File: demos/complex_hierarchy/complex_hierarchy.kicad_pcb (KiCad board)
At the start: 2 copper layers, 72 parts, among them P1 CONN_2, P2 CONN_2, P3 CONN_2, P4 CONN_2, P5 CONN_2, P6 CONN_2, Q1 MPAS92, Q2 MPAS42, Q3 MPAS92, Q4 MPAS42, Q5 MPAS92, Q6 MPAS42, Q7 MPAS92, Q8 MPAS42, U1 ICL7660, U2 78L05, U3 LM358N, U4 LM358N

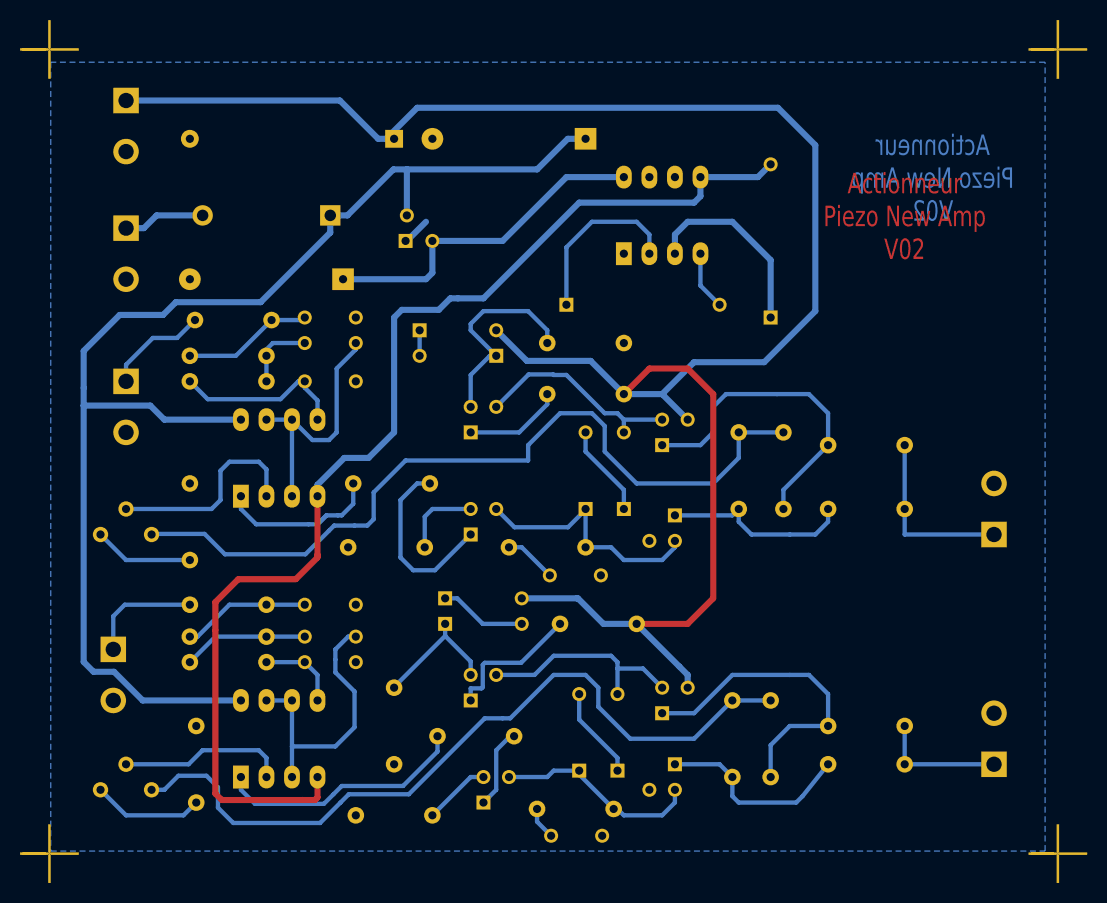
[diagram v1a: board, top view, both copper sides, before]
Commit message: Update demo files. A minor code cleaning.
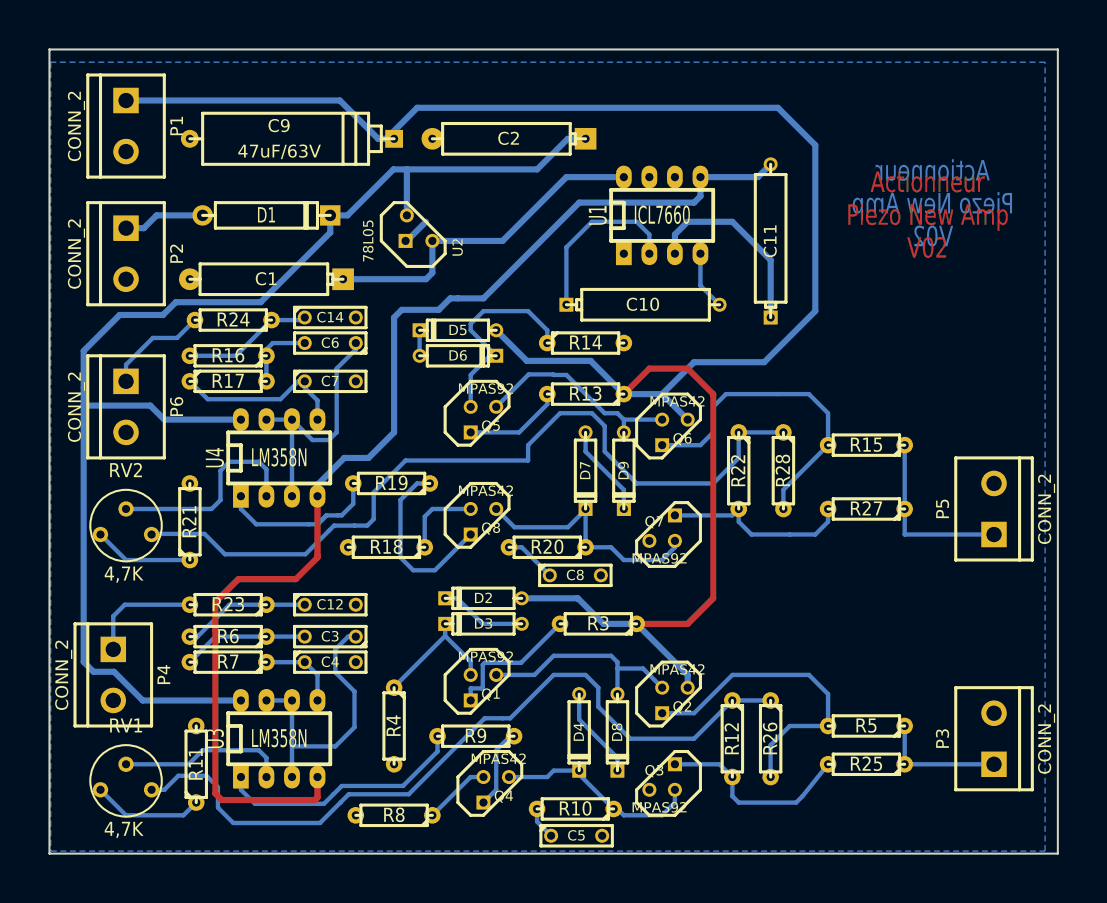
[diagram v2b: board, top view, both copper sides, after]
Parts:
- removed MIRE (x4): *, MIRE
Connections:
- net /ampli_h1 renamed /ampli_ht_vertical/Vpil_0_3,3V
- net /ampli_h2 renamed /ampli_ht_horizontal/Vpil_0_3,3V
- net /ampli_h3 renamed /ampli_ht_vertical/PIEZO_OUT
- net /ampli_h4 renamed /ampli_ht_vertical/PIEZO_IN
- net /ampli_h5 renamed /ampli_ht_horizontal/PIEZO_OUT
- net /ampli_h6 renamed /ampli_ht_horizontal/PIEZO_IN
- net /ampli_h7 renamed /ampli_ht_vertical/S_OUT+
- net /ampli_h8 renamed /ampli_ht_horizontal/S_OUT+
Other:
- board outline added: 100.3 x 80 mm

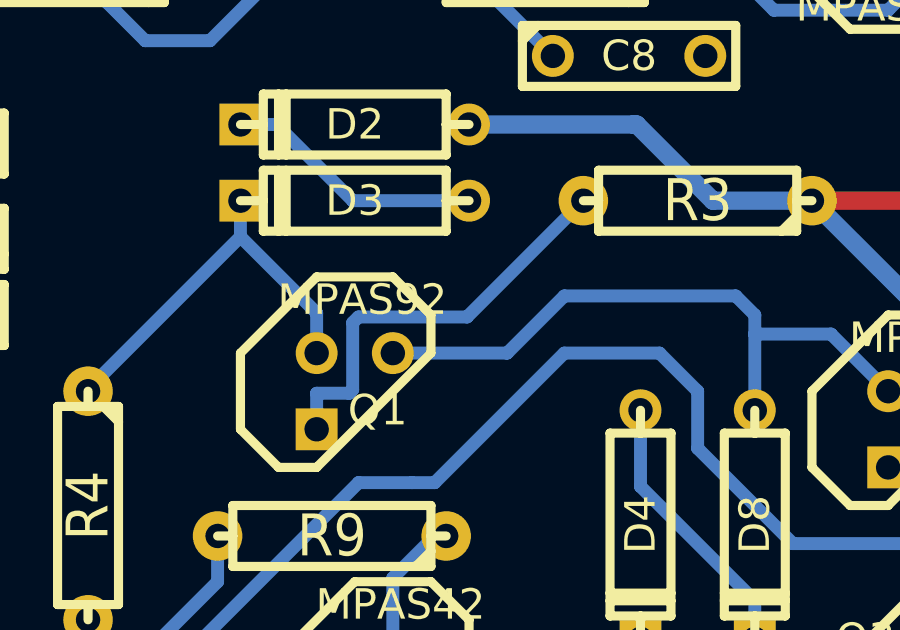
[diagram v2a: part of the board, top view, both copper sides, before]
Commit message: add patch from Cirilo Bernardo, and minor fixes.
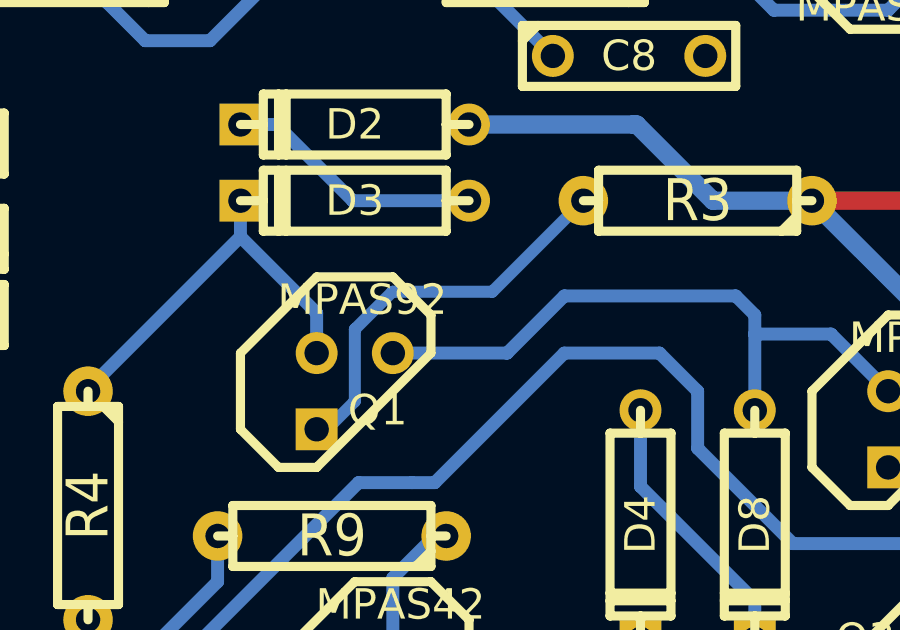
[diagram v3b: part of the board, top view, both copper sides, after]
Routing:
- net Net-(Q1-PadE): track 14.1 -> 13.5 mm
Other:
- net class Default: clearance 0.2794 -> 0.3; trace_width 0.4318 -> 0.4
- net class power: clearance 0.381 -> 0.3; trace_width 0.6096 -> 0.6
- rule trace_clearance: 0.2794 -> 0.3
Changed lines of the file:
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@@
-(kicad_pcb (version 3) (host pcbnew "(2014-01-08 BZR 4616)-product")
+(kicad_pcb (version 3) (host pcbnew "(2014-01-22 BZR 4630)-product")
   (general
     (links 112)
     (no_connects 0)
-    (area 88.163399 51.714399 188.696601 131.927601)
+    (area 84.538458 51.714399 192.321543 131.927601)
     (thickness 1.6002)
     (drawings 6)
-    (tracks 361)
+    (tracks 360)
     (zones 0)
     (modules 68)
@@
   )
   (setup
-    (last_trace_width 0.4318)
-    (trace_clearance 0.2794)
+    (last_trace_width 0.4)
+    (trace_clearance 0.3)
     (zone_clearance 0.508)
     (zone_45_only no)
     (trace_min 0.2032)
-    (segment_width 0.381)
-    (edge_width 0.2032)
+    (segment_width 0.3)
+    (edge_width 0.1)
     (via_size 1.651)
     (via_drill 0.635)
@@
     (uvia_min_size 0.508)
     (uvia_min_drill 0.2032)
-    (pcb_text_width 0.3048)
-    (pcb_text_size 1.524 2.032)
-    (mod_edge_width 0.381)
-    (mod_text_size 1.524 1.524)
-    (mod_text_width 0.3048)
+    (pcb_text_width 0.3)
+    (pcb_text_size 2 2)
+    (mod_edge_width 0.2)
+    (mod_text_size 1 1)
+    (mod_text_width 0.2)
     (pad_size 2.286 2.286)
     (pad_drill 0.8128)
@@
   (net 50 VCC)
   (net_class Default "Ceci est la Netclass par défaut"
-    (clearance 0.2794)
-    (trace_width 0.4318)
+    (clearance 0.3)
+    (trace_width 0.4)
     (via_dia 1.651)
     (via_drill 0.635)
@@
   )
   (net_class power ""
-    (clearance 0.381)
-    (trace_width 0.6096)
+    (clearance 0.3)
+    (trace_width 0.6)
     (via_dia 1.651)
     (via_drill 0.635)
@@
   (segment (start 145.415 89.916) (end 145.415 88.646) (width 0.4318) (layer Cuivre) (net 33) (status 800))
   (segment (start 145.415 88.646) (end 149.225 88.646) (width 0.4318) (layer Cuivre) (net 33) (status 400))
-  (segment (start 135.18896 112.84204) (end 139.065 108.966) (width 0.4318) (layer Cuivre) (net 34) (status 400))
-  (segment (start 131.56692 112.84204) (end 135.18896 112.84204) (width 0.4318) (layer Cuivre) (net 34))
-  (segment (start 131.37642 115.26266) (end 131.37642 113.03254) (width 0.4318) (layer Cuivre) (net 34))
-  (segment (start 130.175 116.586) (end 130.175 115.38458) (width 0.4318) (layer Cuivre) (net 34) (status 800))
-  (segment (start 131.2545 115.38458) (end 131.37642 115.26266) (width 0.4318) (layer Cuivre) (net 34))
-  (segment (start 131.37642 113.03254) (end 131.56692 112.84204) (width 0.4318) (layer Cuivre) (net 34))
-  (segment (start 130.175 115.38458) (end 131.2545 115.38458) (width 0.4318) (layer Cuivre) (net 34))
+  (segment (start 130.175 116.586) (end 130.514 116.586) (width 0.4) (layer Cuivre) (net 34))
+  (segment (start 136.031 112) (end 139.065 108.966) (width 0.4) (layer Cuivre) (net 34))
+  (segment (start 132.7 112) (end 136.031 112) (width 0.4) (layer Cuivre) (net 34))
+  (segment (start 131.44787 113.25213) (end 132.7 112) (width 0.4) (layer Cuivre) (net 34))
+  (segment (start 131.44787 115.65213) (end 131.44787 113.25213) (width 0.4) (layer Cuivre) (net 34))
+  (segment (start 130.514 116.586) (end 131.44787 115.65213) (width 0.4) (layer Cuivre) (net 34))
   (segment (start 160.02 124.206) (end 160.02 121.031) (width 0.4318) (layer Cuivre) (net 35) (status 800))
   (segment (start 161.925 119.126) (end 165.735 119.126) (width 0.4318) (layer Cuivre) (net 35) (status 400))

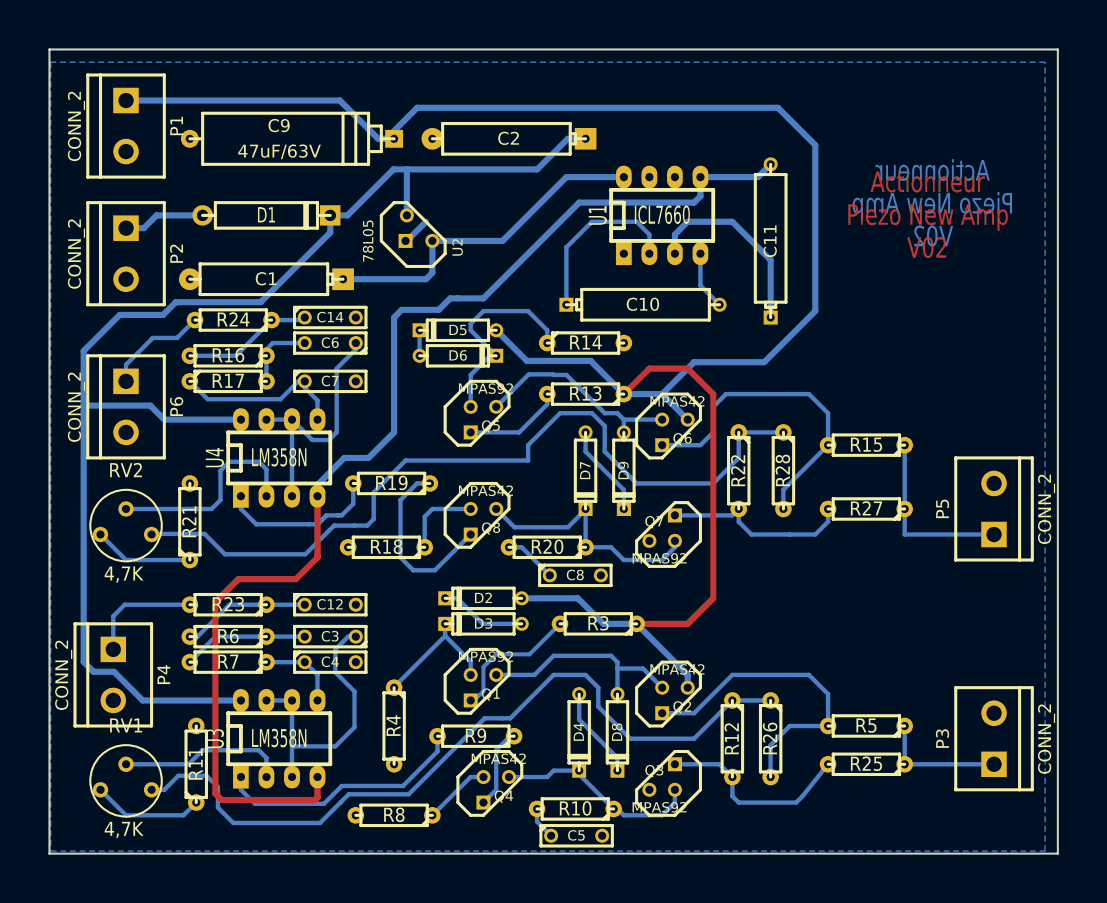
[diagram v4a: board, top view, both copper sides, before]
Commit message: Eeschema: BOM dialog: fix some minor issues when displaying messages. Cvpcb: fix Bug #1470201 (select next/previous unlinked comp and clear links not working well) demo/complex_hierarchy: use our new schematic symbols.
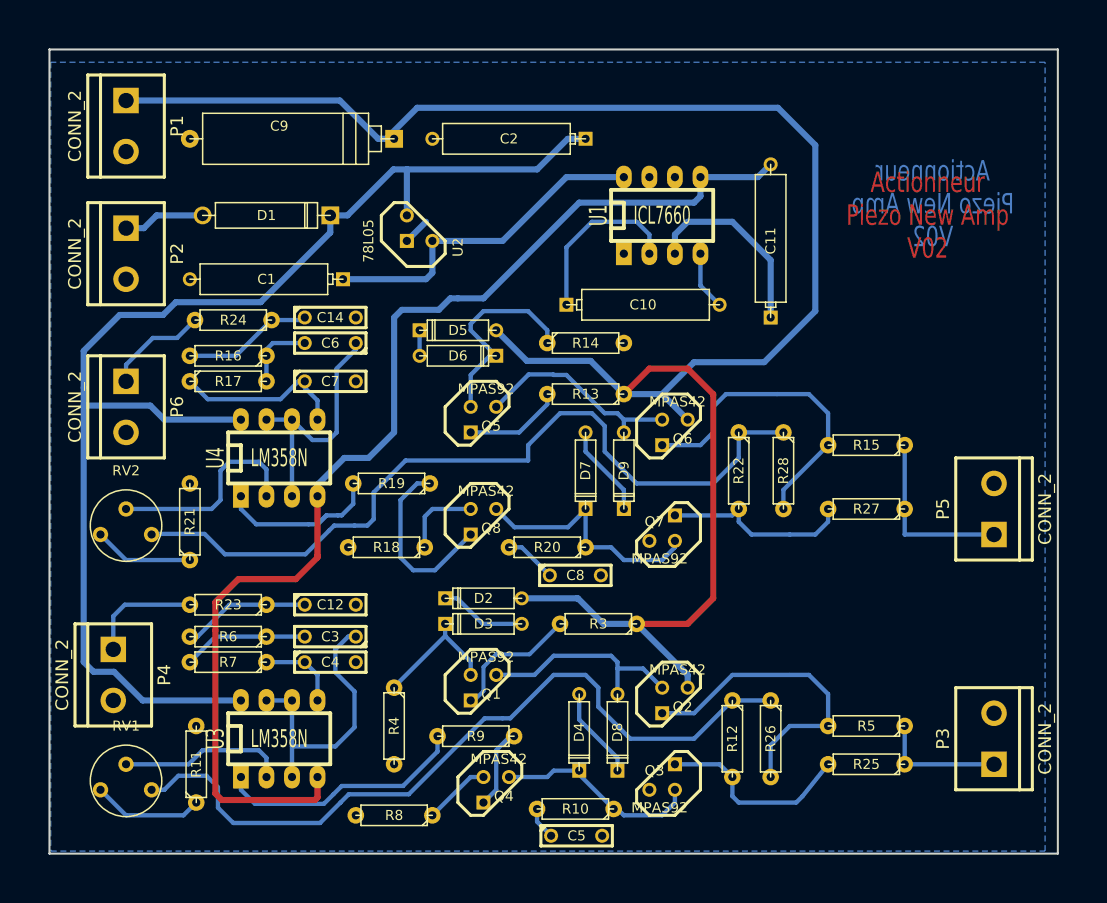
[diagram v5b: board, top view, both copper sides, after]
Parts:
- C1, C10, C11, C2: footprint CP6 -> discret:CP6
- C12, C14, C3, C5, C6, C8: footprint C2 -> discret:C2
- C4, C7: value 4,7nF -> 4.7nF; footprint C2 -> discret:C2
- C9: footprint CP8 -> discret:CP8
- D1: footprint D5 -> discret:D5
- D2, D3, D4, D5, D6, D7, D8, D9: footprint D3 -> discret:D3
- P1, P2, P3, P4, P5, P6: footprint bornier2 -> connect:bornier2
- Q1, Q2, Q3, Q4, Q5, Q6, Q7, Q8: footprint TO92-CBE -> discret:TO92-CBE
- R10, R11, R12, R13, R14, R15, R16, R17, R18, R19, R20, R21, R22, R23, R24, R25, R26, R27, R28, R3, R4, R5, R6, R7, R8, R9: footprint R3-LARGE_PADS -> discret:R3-LARGE_PADS
- RV1, RV2: footprint RV2 -> discret:RV2
- U1, U3, U4: footprint DIP-8__300_ELL -> dip_sockets:DIP-8__300_ELL
- U2: footprint LM78LXX -> discret:LM78LXX
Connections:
- D1 pad 1: /12Vext -> +12V
- D1 pad 2: +12V -> /12Vext
- D2 pad 1: HT -> Net-(D2-Pad1)
- D2 pad 2: Net-(D2-Pad2) -> HT
- D3 pad 1: Net-(D2-Pad2) -> Net-(D3-Pad1)
- D3 pad 2: Net-(D3-Pad2) -> Net-(D2-Pad1)
- D5 pad 1: HT -> Net-(D5-Pad1)
- D5 pad 2: Net-(D5-Pad2) -> HT
- D6 pad 1: Net-(D5-Pad2) -> Net-(D6-Pad1)
- D6 pad 2: Net-(D6-Pad2) -> Net-(D5-Pad1)
- D8 pad 1: Net-(D8-Pad1) -> Net-(D4-Pad2)
- D8 pad 2: Net-(D4-Pad1) -> Net-(D8-Pad2)
- D9 pad 1: Net-(D9-Pad1) -> Net-(D7-Pad2)
- D9 pad 2: Net-(D7-Pad1) -> Net-(D9-Pad2)
- Q1 pad B: Net-(D3-Pad2) -> Net-(D3-Pad1)
- Q1 pad C: Net-(D8-Pad1) -> Net-(D8-Pad2)
- Q2 pad B: Net-(D8-Pad1) -> Net-(D8-Pad2)
- Q3 pad B: Net-(D4-Pad2) -> Net-(D4-Pad1)
- Q4 pad C: Net-(D4-Pad2) -> Net-(D4-Pad1)
- Q5 pad B: Net-(D6-Pad2) -> Net-(D6-Pad1)
- Q5 pad C: Net-(D9-Pad1) -> Net-(D9-Pad2)
- Q6 pad B: Net-(D9-Pad1) -> Net-(D9-Pad2)
- Q7 pad B: Net-(D7-Pad2) -> Net-(D7-Pad1)
- Q8 pad C: Net-(D7-Pad2) -> Net-(D7-Pad1)
- R10 pad 1: Net-(D4-Pad2) -> Net-(D4-Pad1)
- R14 pad 1: Net-(D6-Pad2) -> Net-(D6-Pad1)
- R20 pad 1: Net-(D7-Pad2) -> Net-(D7-Pad1)
- R4 pad 1: Net-(D3-Pad2) -> Net-(D3-Pad1)
- U1 pad 6: (no net) -> Net-(U1-Pad6)
- U1 pad 7: (no net) -> Net-(U1-Pad7)
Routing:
- net Net-(D8-Pad2): track 0.00 -> 21.5 mm
- net Net-(D8-Pad1): track 21.5 -> 0.00 mm
- net Net-(D9-Pad2): track 0.00 -> 21.0 mm
- net Net-(D9-Pad1): track 21.0 -> 0.00 mm
- net Net-(D6-Pad2): track 20.9 -> 0.00 mm
- net Net-(D6-Pad1): track 0.00 -> 20.9 mm
- net Net-(D7-Pad2): track 24.9 -> 9.20 mm
- net Net-(D7-Pad1): track 9.20 -> 24.9 mm
- net Net-(D3-Pad2): track 13.4 -> 0.00 mm
- net Net-(D3-Pad1): track 0.00 -> 13.4 mm
- net Net-(D4-Pad2): track 20.6 -> 9.20 mm
- net Net-(D4-Pad1): track 9.20 -> 20.6 mm
- net Net-(D2-Pad2): track 8.67 -> 0.00 mm
- net Net-(D2-Pad1): track 0.00 -> 8.67 mm
- net Net-(D5-Pad2): track 2.54 -> 0.00 mm
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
